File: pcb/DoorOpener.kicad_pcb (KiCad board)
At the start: 2 copper layers, 90.9 x 68.1 mm, 19 parts, among them J1 Serial, J2 Serial, J3 14V, SW1 POWER, SW2 Button, SW4 Button, SW5 Reset, U1 ESP-01v090, U2 ESP-01v090, U3 dcdc, U4 Relay

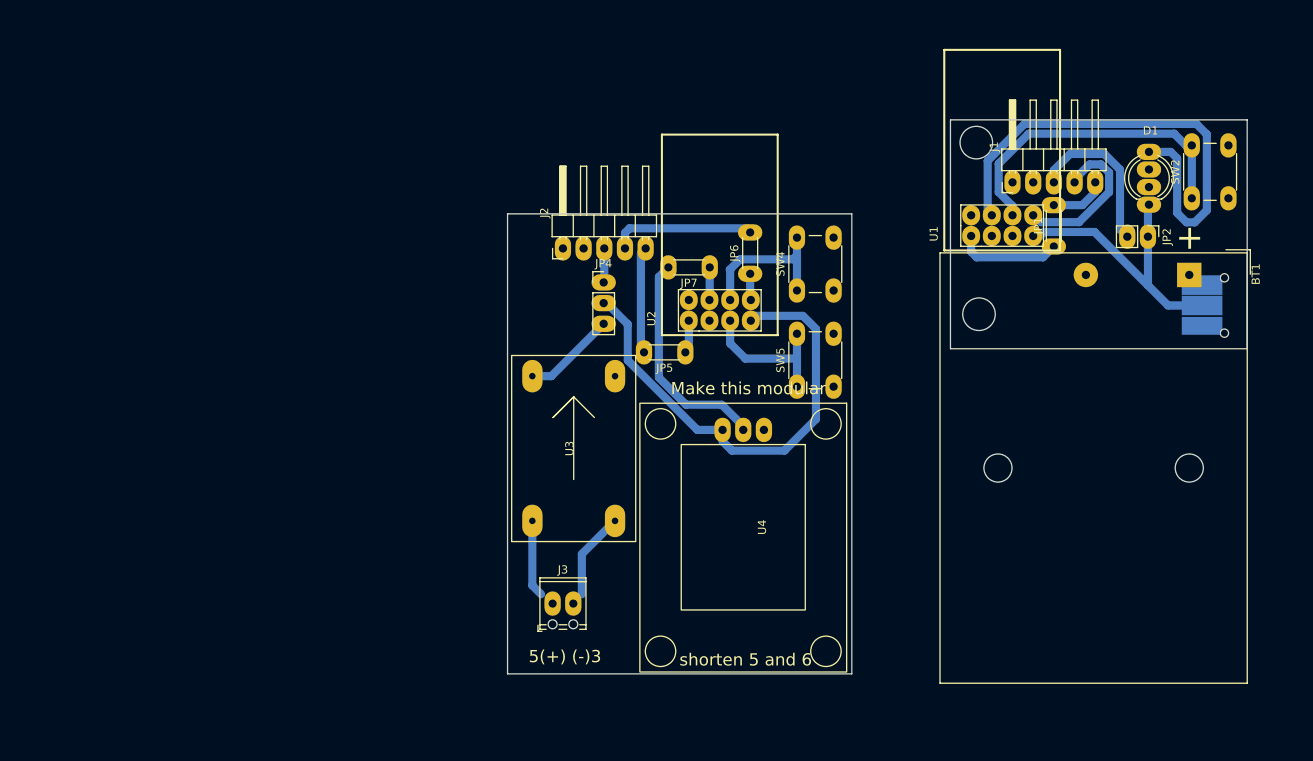
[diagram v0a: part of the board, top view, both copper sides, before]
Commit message: Update PCB with the housing constraints
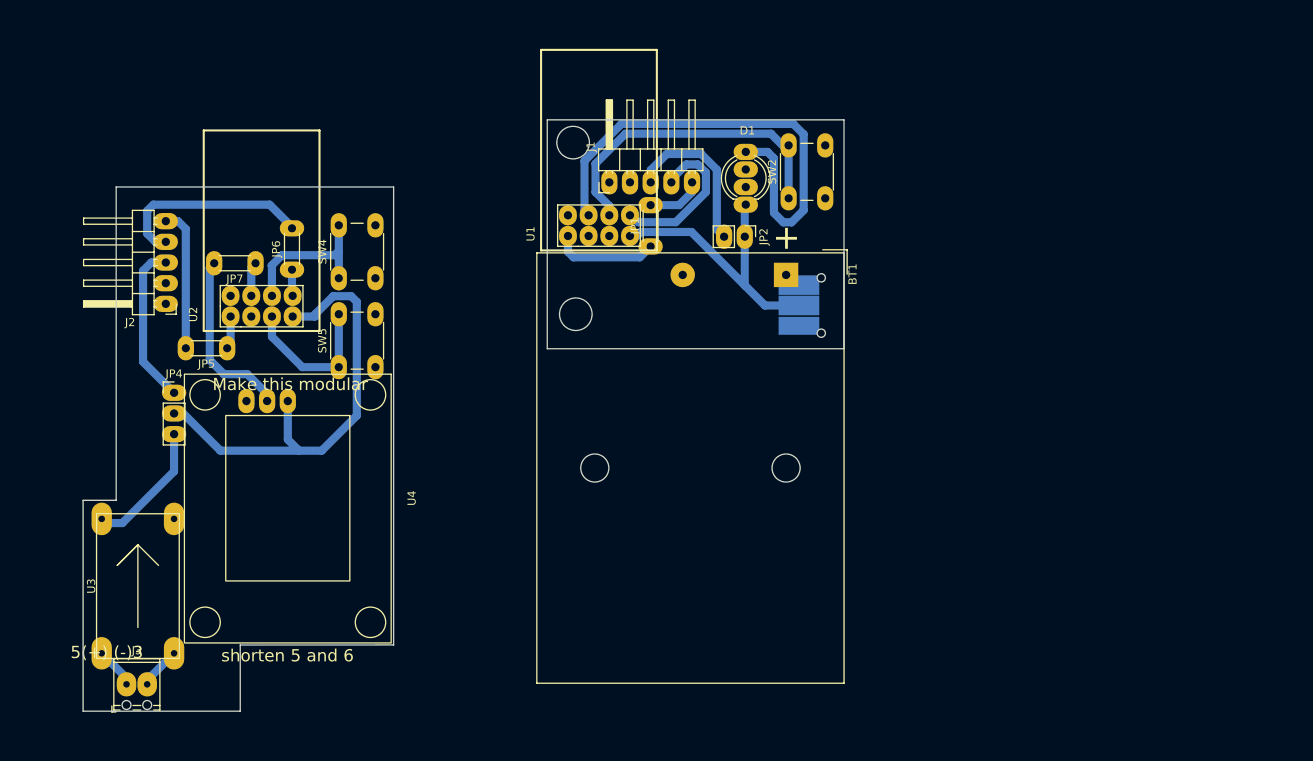
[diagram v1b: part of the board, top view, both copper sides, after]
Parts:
- U4: value Relay -> relais_module
- moved SW5 56.3 mm to (131.0, 58.3)
- moved SW4 56.3 mm to (131.0, 47.4)
- moved JP5 56.3 mm to (117.3, 56.0)
- moved U2 56.3 mm to (117.7, 52.1)
- moved JP6 56.3 mm to (125.2, 46.3)
- moved U3 56.1 mm to (106.3, 85.2)
- moved U4 56.1 mm to (124.7, 74.4)
- moved JP7 55.8 mm to (120.8, 45.6)
- moved JP4 54.5 mm to (110.7, 61.5)
- moved J3 53.3 mm to (104.9, 97.3)
- moved BT1 49.5 mm to (185.9, 47.0)
- moved D1 49.5 mm to (181.0, 38.4)
- moved J1 49.5 mm to (164.2, 35.6)
- moved JP1 49.5 mm to (169.3, 43.5)
- moved JP2 49.5 mm to (180.9, 42.3)
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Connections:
- J2 pad 2: (no net) -> unconnected-(J2-Pad2)
- J2 pad 3: (no net) -> /FTDI_3V3
- J2 pad 4: (no net) -> Net-(J2-Pad4)
- J2 pad 5: (no net) -> Net-(J2-Pad5)
- J3 pad 1: (no net) -> Net-(J3-Pad1)
- J3 pad 2: (no net) -> Net-(J3-Pad2)
- JP4 pad 1: (no net) -> /FTDI_3V3
- JP4 pad 3: (no net) -> Net-(JP4-Pad3)
- JP5 pad 2: (no net) -> Net-(J2-Pad5)
- JP6 pad 2: (no net) -> Net-(J2-Pad4)
- JP7 pad 1: (no net) -> Net-(JP7-Pad1)
- JP7 pad 2: (no net) -> Net-(JP7-Pad2)
- SW4 pad 1: (no net) -> Net-(SW4-Pad1)
- SW5 pad 1: (no net) -> Net-(SW5-Pad1)
- U2 pad 3: (no net) -> unconnected-(U2-Pad3)
- U2 pad 4: (no net) -> Net-(JP7-Pad1)
- U2 pad 5: (no net) -> Net-(SW5-Pad1)
- U2 pad 6: (no net) -> Net-(SW4-Pad1)
- U3 pad 1: (no net) -> Net-(J3-Pad2)
- U3 pad 2: (no net) -> Net-(J3-Pad1)
- U3 pad 3: (no net) -> Net-(JP4-Pad3)
- U4 pad 2: (no net) -> Net-(JP7-Pad2)
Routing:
- net (no net): track 134.6 -> 0.00 mm
- net Net-(J2-Pad4): track 0.00 -> 24.7 mm
- net Net-(JP7-Pad2): track 0.00 -> 21.8 mm
- net /FTDI_3V3: track 0.00 -> 19.8 mm
- net Net-(SW4-Pad1): track 0.00 -> 19.2 mm
- net Net-(SW5-Pad1): track 0.00 -> 18.7 mm
- net Net-(J2-Pad5): track 0.00 -> 17.8 mm
- net Net-(JP4-Pad3): track 0.00 -> 16.1 mm
- net Net-(J3-Pad1): track 0.00 -> 5.18 mm
- net Net-(J3-Pad2): track 0.00 -> 5.07 mm
- net Net-(JP7-Pad1): track 0.00 -> 4.22 mm
- net +3V3: track 93.3 -> 90.8 mm
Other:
- board size 90.9 x 68.1 mm -> 93.5 x 72.6 mm

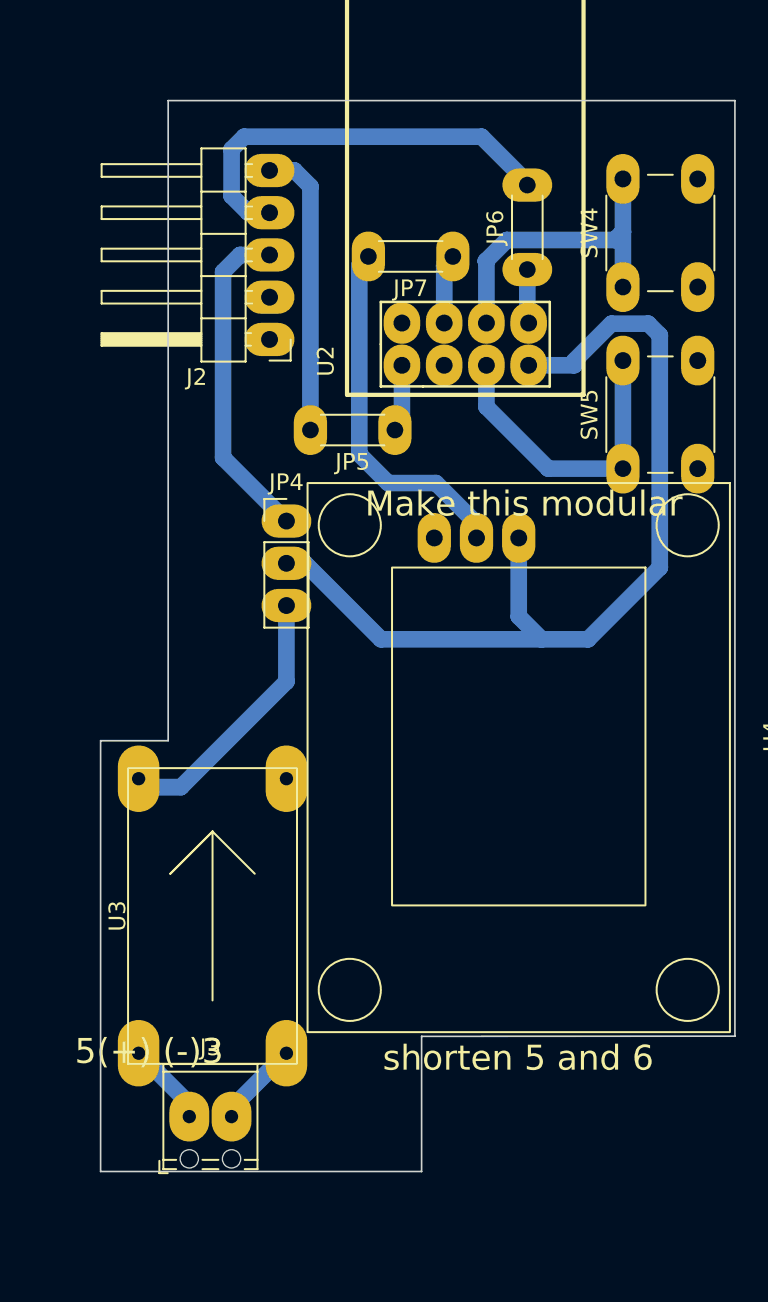
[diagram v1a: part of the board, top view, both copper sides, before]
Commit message: Update terminal socket footprint and some minor changes
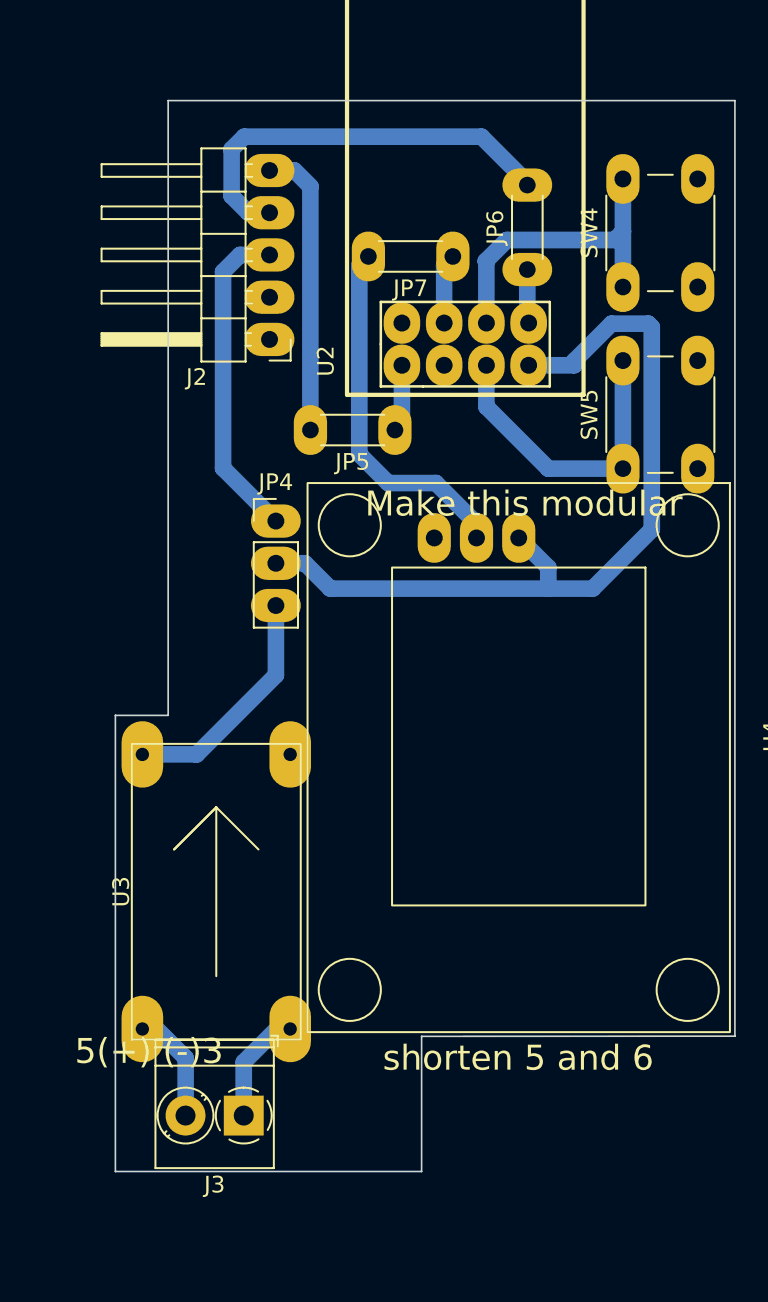
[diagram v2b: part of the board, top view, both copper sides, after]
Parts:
- J3: footprint TerminalBlock_Phoenix:TerminalBlock_Phoenix_MPT-0,5-2-2.54_1x02_P2.54mm_Horizontal -> TerminalBlock_Phoenix:TerminalBlock_Phoenix_PT-1,5-2-3.5-H_1x02_P3.50mm_Horizontal
- U4: value relais_module -> Relay
- moved J3 3.27 mm to (108.2, 97.2), turned to 180 degrees
- moved U3 1.48 mm to (106.5, 83.8)
- moved JP4 0.64 mm to (110.1, 61.5)
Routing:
- net +3V3: track 90.8 -> 84.0 mm
- net Net-(JP4-Pad3): track 16.1 -> 14.2 mm
- net Net-(J3-Pad2): track 5.07 -> 6.78 mm
- net Net-(J3-Pad1): track 5.18 -> 6.83 mm
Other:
- board size 93.5 x 72.6 mm -> 92.6 x 72.6 mm

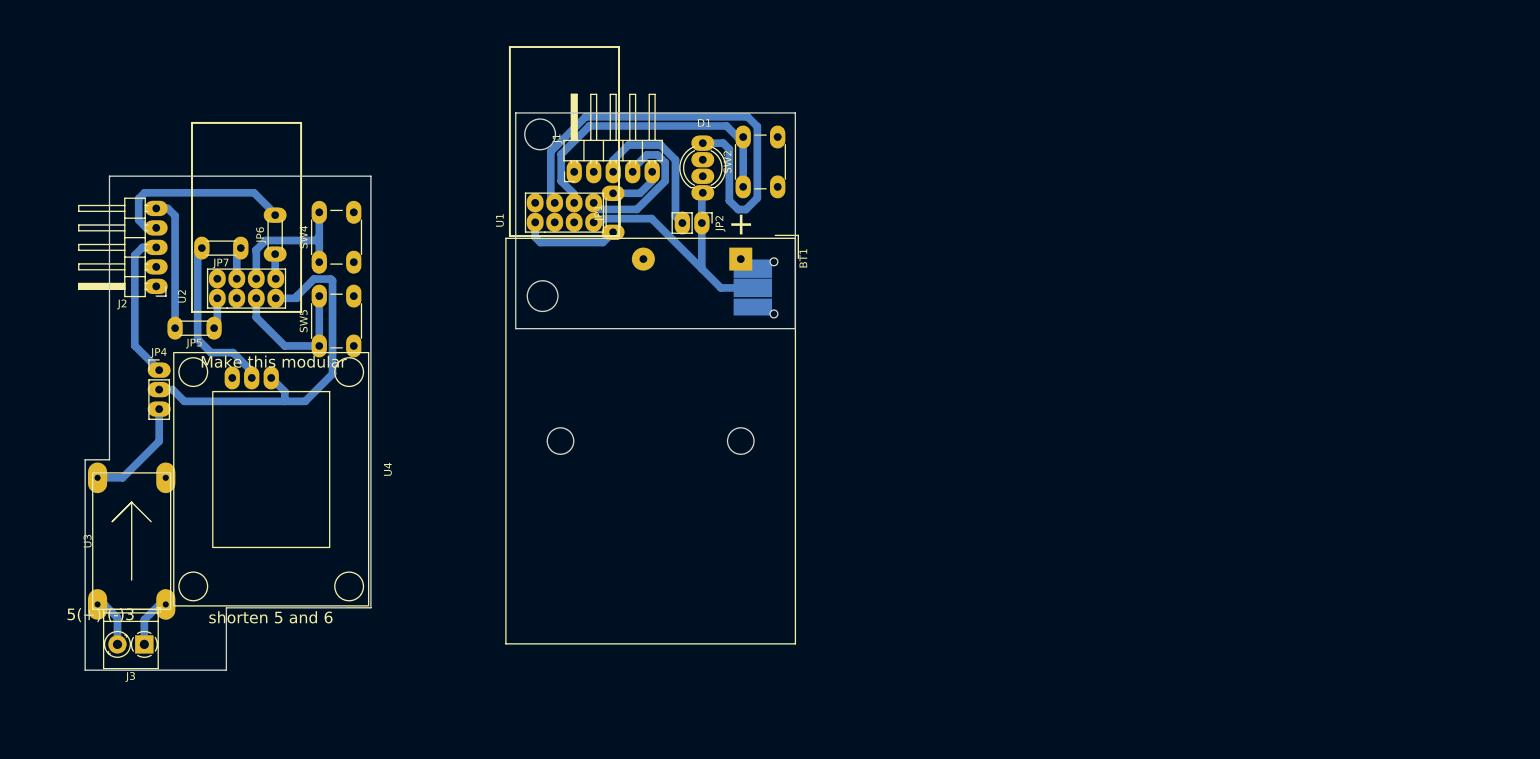
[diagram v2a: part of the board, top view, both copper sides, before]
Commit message: Swap VCC and Signal pin
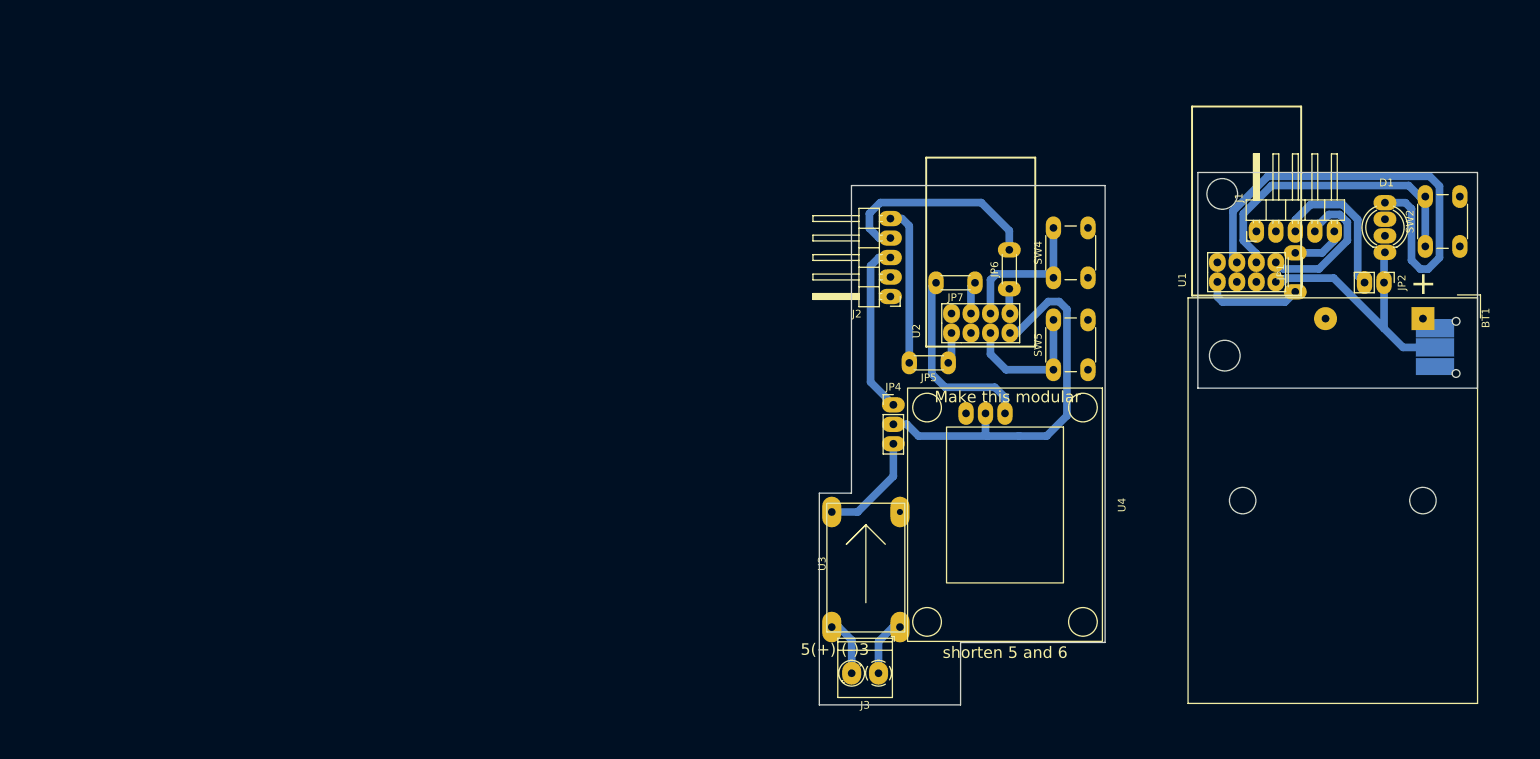
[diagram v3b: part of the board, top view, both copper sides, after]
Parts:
- U4: value Relay -> relais_module
- moved JP4 95.8 mm to (205.8, 66.0)
- moved JP6 95.8 mm to (220.9, 50.9)
- moved JP7 95.8 mm to (216.5, 50.1)
- moved JP5 95.8 mm to (213.0, 60.5)
- moved U2 95.8 mm to (213.4, 56.6)
- moved J3 95.8 mm to (203.9, 101.0)
- moved U4 95.8 mm to (220.4, 79.0)
- moved SW5 95.8 mm to (226.7, 61.4)
- moved U3 95.8 mm to (202.2, 86.7)
- moved SW4 95.7 mm to (226.7, 49.4)
- moved J2 95.7 mm to (205.4, 51.9)
- moved D1 89.3 mm to (269.9, 46.1)
- moved SW2 89.3 mm to (275.2, 45.3)
- moved BT1 89.3 mm to (274.9, 54.8)
- moved J1 89.3 mm to (253.1, 43.4)
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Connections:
- J3 pad 1: Net-(J3-Pad1) -> GND
- U3 pad 2: Net-(J3-Pad1) -> GND
- U4 pad 2: Net-(JP7-Pad2) -> +3V3
- U4 pad 3: +3V3 -> Net-(JP7-Pad2)
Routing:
- net GND: track 0.00 -> 7.70 mm
- net Net-(J3-Pad1): track 6.83 -> 0.00 mm
- net Net-(J2-Pad4): track 24.7 -> 28.0 mm
- net Net-(JP7-Pad2): track 21.8 -> 25.0 mm
- net Net-(J2-Pad5): track 17.8 -> 21.0 mm
- net /FTDI_3V3: track 19.5 -> 22.4 mm
- net +3V3: track 84.0 -> 86.3 mm
- net Net-(J3-Pad2): track 6.78 -> 7.63 mm
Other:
- board size 92.6 x 72.6 mm -> 85.8 x 69.4 mm

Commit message: Fix wrong polarity of the dcdc module and replace the relais circuit
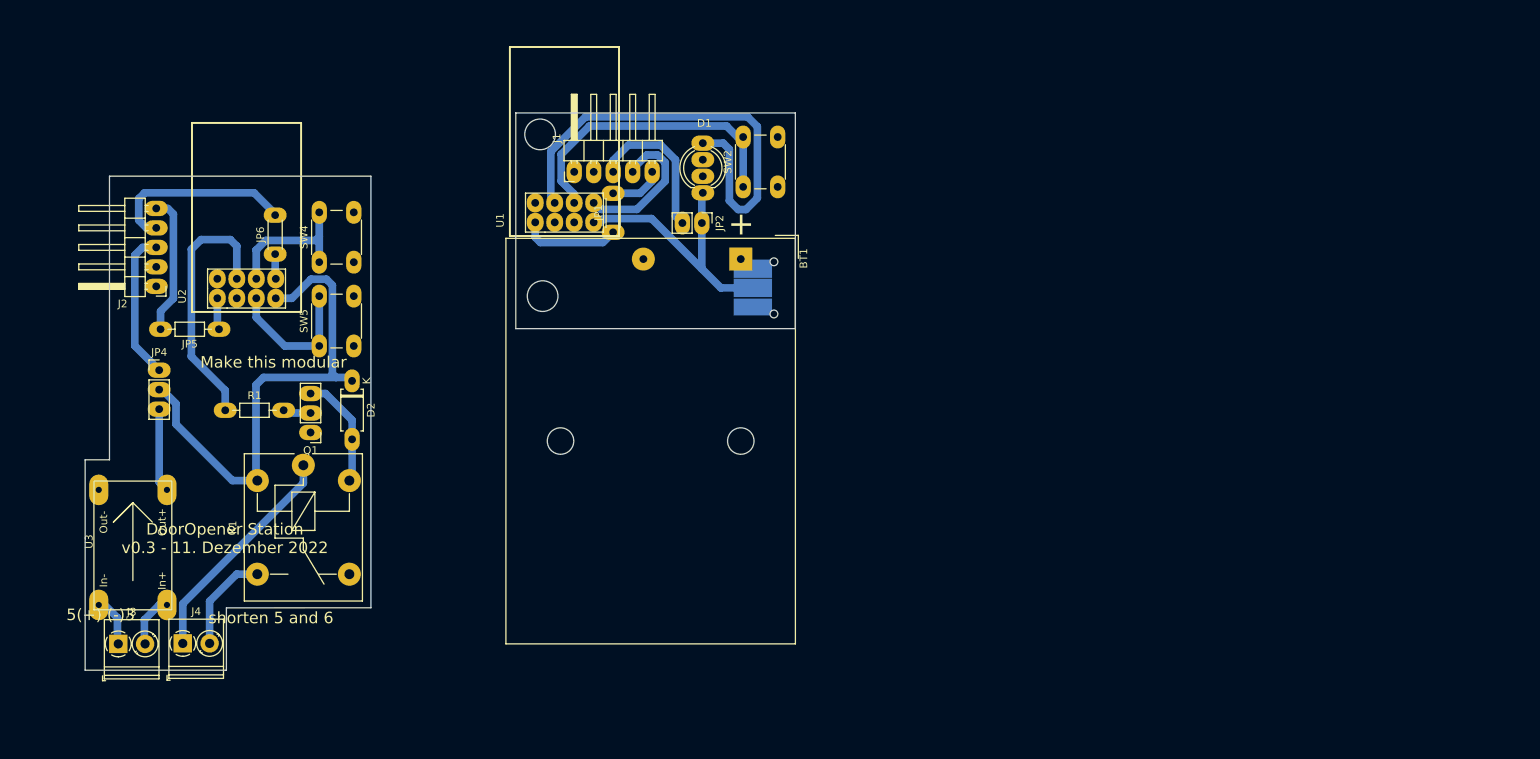
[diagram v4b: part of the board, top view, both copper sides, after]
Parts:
- removed JP7: Bridge, Resistor_THT:R_Axial_DIN0204_L3.6mm_D1.6mm_P5.08mm_Horizontal
- removed U4: relais_module, relais_module:relais_module
- added D2: D_Small, Diode_THT:D_A-405_P7.62mm_Horizontal, F.Cu at (135.3, 62.9)
- added J4: 14V, TerminalBlock_Phoenix:TerminalBlock_Phoenix_PT-1,5-2-3.5-H_1x02_P3.50mm_Horizontal, F.Cu at (113.2, 97.1)
- added K1: FINDER-36.11, Relay_THT:Relay_SPDT_Finder_36.11, F.Cu at (128.9, 73.9)
- added Q1: 2N2219, Connector_PinHeader_2.54mm:PinHeader_1x03_P2.54mm_Vertical, F.Cu at (129.8, 69.6)
- added R1: R, Resistor_THT:R_Axial_DIN0204_L3.6mm_D1.6mm_P7.62mm_Horizontal, F.Cu at (118.7, 66.7)
- JP5: footprint Resistor_THT:R_Axial_DIN0204_L3.6mm_D1.6mm_P5.08mm_Horizontal -> Resistor_THT:R_Axial_DIN0204_L3.6mm_D1.6mm_P7.62mm_Horizontal
- moved J3 99.2 mm to (104.8, 97.2), turned to 0 degrees
- moved JP4 95.8 mm to (110.1, 61.5)
- moved JP6 95.8 mm to (125.2, 46.3)
- moved U2 95.8 mm to (117.7, 52.1)
- moved SW5 95.8 mm to (131.0, 58.3)
- moved SW4 95.7 mm to (131.0, 47.4)
- moved J2 95.7 mm to (109.7, 50.5)
- moved U3 95.6 mm to (106.7, 83.8)
- moved JP5 95.2 mm to (117.9, 56.1)
- moved D1 89.3 mm to (181.0, 38.4)
- moved SW2 89.3 mm to (186.2, 37.6)
- moved BT1 89.3 mm to (185.9, 47.0)
- moved J1 89.3 mm to (164.2, 35.6)
- moved JP1 89.3 mm to (169.3, 43.5)
- moved JP2 89.3 mm to (180.9, 42.3)
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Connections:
- U3 pad 1: Net-(J3-Pad2) -> GND
- U3 pad 2: GND -> Net-(J3-Pad2)
- U3 pad 3: Net-(JP4-Pad3) -> GND
- U3 pad 4: GND -> Net-(JP4-Pad3)
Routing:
- net Net-(K1-Pad11): track 0.00 -> 29.7 mm
- net Net-(U2-Pad4): track 4.22 -> 33.9 mm
- net Net-(JP7-Pad2): track 25.0 -> 0.00 mm
- net Net-(D2-Pad2): track 0.00 -> 14.9 mm
- net +3V3: track 86.3 -> 100.5 mm
- net Net-(K1-Pad14): track 0.00 -> 13.2 mm
- net Net-(Q1-Pad2): track 0.00 -> 3.65 mm
- net Net-(J2-Pad4): track 28.0 -> 24.7 mm
- net Net-(JP4-Pad3): track 14.2 -> 10.9 mm
- net /FTDI_3V3: track 22.4 -> 19.5 mm
- net Net-(J2-Pad5): track 21.0 -> 18.2 mm
- net GND: track 7.70 -> 6.78 mm
- net Net-(J3-Pad2): track 7.63 -> 6.83 mm
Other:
- board size 85.8 x 69.4 mm -> 92.6 x 72.6 mm
- board text added: "DoorOpener Station v0.3 - 11. Dezember 2022"

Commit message: Prepare for 0.3v plot
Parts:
- J4: value 14V -> Terminal
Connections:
- J4 pad 1: Net-(K1-Pad11) -> (no net)
- J4 pad 2: Net-(K1-Pad14) -> (no net)
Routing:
- net Net-(JP4-Pad3): track 10.9 -> 11.9 mm
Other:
- board text removed: "Make this modular"
